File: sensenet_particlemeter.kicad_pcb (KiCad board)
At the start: 2 copper layers, 63.6 x 72.3 mm, 92 parts, among them J1 CONN_01X01, J10 CONN_01X01, J11 CONN_01X01, J12 CONN_01X01, J13 BARREL_JACK, J14 CONN_01X01, J15 CONN_01X01, J16 CONN_01X01, J17 CONN_01X01, J18 CONN_01X01, J19 CONN_01X01, J2 CONN_01X01, J20 CONN_01X01, J3 CONN_01X01, J4 CONN_01X01, J5 CONN_01X01, J6 CONN_01X01, J7 CONN_01X06, J8 CONN_01X01, J9 CONN_01X01, P1 SMA_mini, P2 SMA_mini, Q1 Q_NPN_BCV71, SW1 SW_Push, U1 wireless_patice, U10 bme280_barebone, U11 SR4G008, U2 stm32f072, U3 QUECTEL_BC95, U4 SIM, U6 M24C04, U7 M10578-A2, U8 LD39050, U9 NCP59150, Y1 8MHz

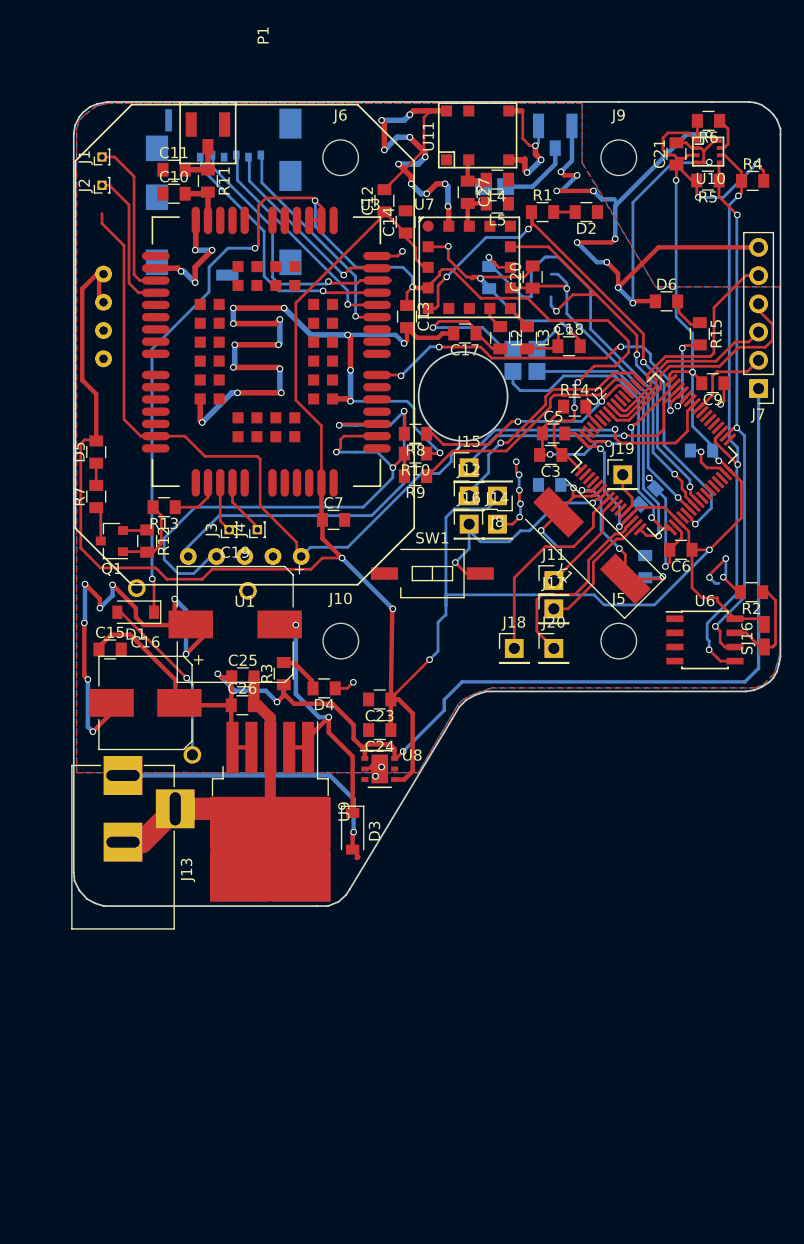
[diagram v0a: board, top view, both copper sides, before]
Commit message: added reset pin wire for quectel, fixed holes position
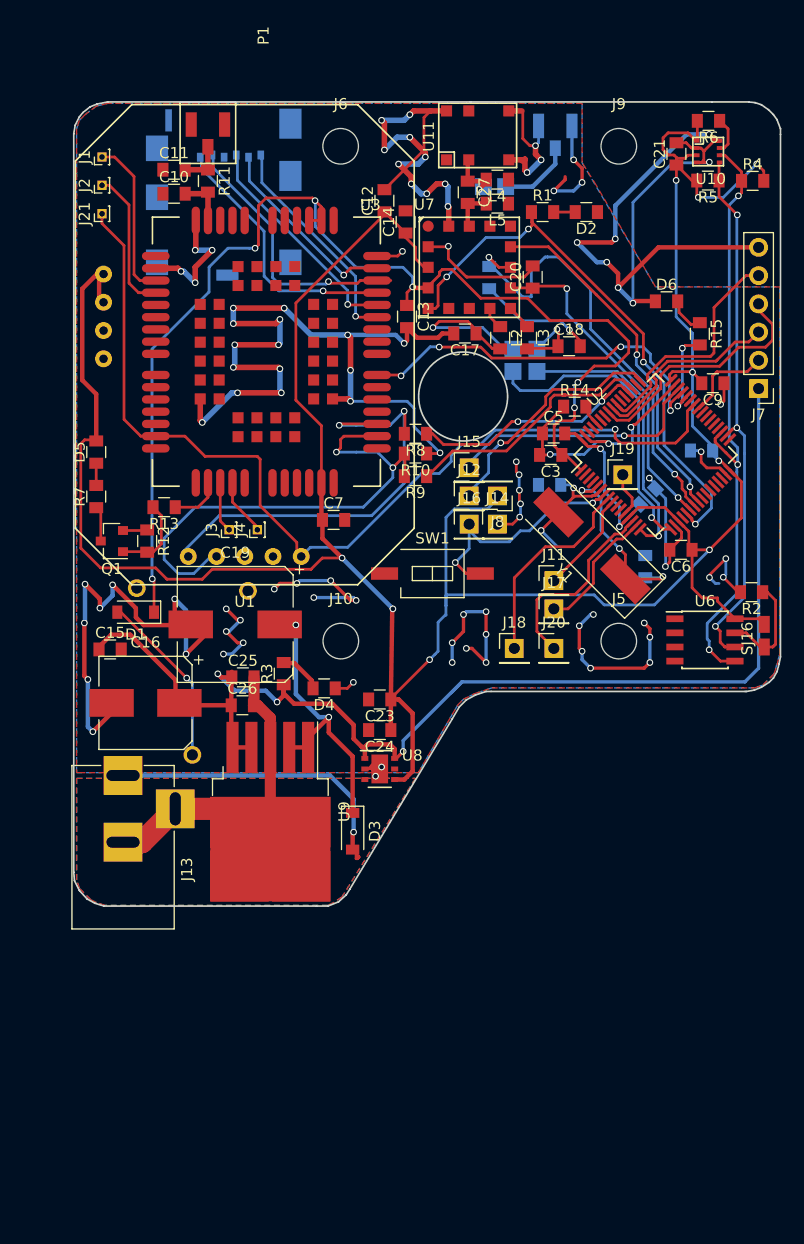
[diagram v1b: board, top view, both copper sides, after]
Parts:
- added J21: CONN_01X01, SNPM:Pin_Header_Straight_1x01_Pitch1.00mm, F.Cu at (134.6, 63.5)
- moved J6 1.03 mm to (156.1, 57.5)
- moved J9 1.03 mm to (181.1, 57.5)
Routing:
- net (no net): track 0.00 -> 48.8 mm, vias 0 -> 24
- net GND: track 408.6 -> 399.0 mm, vias 74 -> 72
- net +5V: track 112.3 -> 119.8 mm
- net gps_pulses: track 37.7 -> 32.0 mm, vias 3 -> 2
- net gps_standby: track 32.0 -> 29.8 mm
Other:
- net class Default: trace_width 0.25 -> 0.3

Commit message: lorawan module PCB added
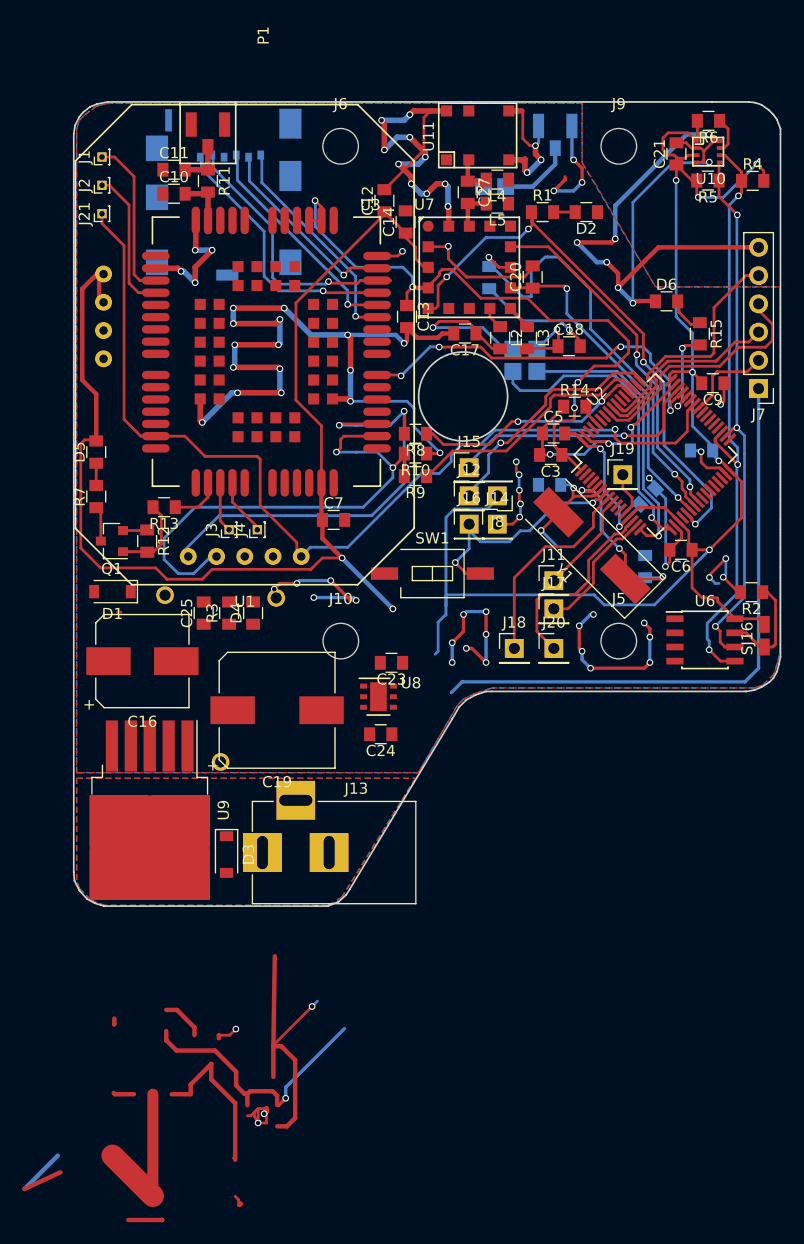
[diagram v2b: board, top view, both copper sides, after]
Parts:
- removed C15: 1u, SNPM:SMD_0805
- removed C26: 220n, SNPM:SMD_0805
- C16: value 470u -> 220n
- C19: value 220u -> 470u
- C23, C25: value 1u -> 10u
- moved J13 14.3 mm to (149.0, 121.0), turned to 180 degrees
- moved D3 11.5 mm to (145.8, 121.2)
- moved U9 10.8 mm to (138.9, 117.2)
- moved D4 9.31 mm to (148.2, 99.4), turned to 90 degrees
- moved C19 8.59 mm to (150.4, 108.2), turned to 0 degrees
- moved R3 7.34 mm to (146.1, 99.4)
- moved C25 6.77 mm to (143.8, 99.4), turned to 90 degrees
- moved U8 6.50 mm to (159.5, 107.0)
- moved C16 3.77 mm to (138.3, 103.8), turned to 0 degrees
- moved C23 3.46 mm to (160.7, 103.9)
- moved D1 2.79 mm to (135.6, 97.5)
- moved BT1 2.62 mm to (145.3, 108.1)
- moved C24 0.39 mm to (159.7, 110.3)
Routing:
- net (no net): track 48.8 -> 162.4 mm
- net GND: track 399.0 -> 299.2 mm, vias 72 -> 61
- net +5V: track 119.8 -> 53.7 mm, vias 3 -> 0
- net batt: track 107.1 -> 59.6 mm, vias 6 -> 4
- net Net-(C19-Pad1): track 29.2 -> 0.00 mm, vias 2 -> 0
- net Net-(D3-Pad2): track 27.7 -> 0.00 mm, vias 1 -> 0
- net +3V3: track 281.2 -> 255.0 mm, vias 11 -> 10
- net Net-(BT1-Pad1): track 15.8 -> 0.00 mm, vias 1 -> 0
- net Net-(D4-Pad2): track 3.88 -> 0.00 mm

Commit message: reorganized power connections
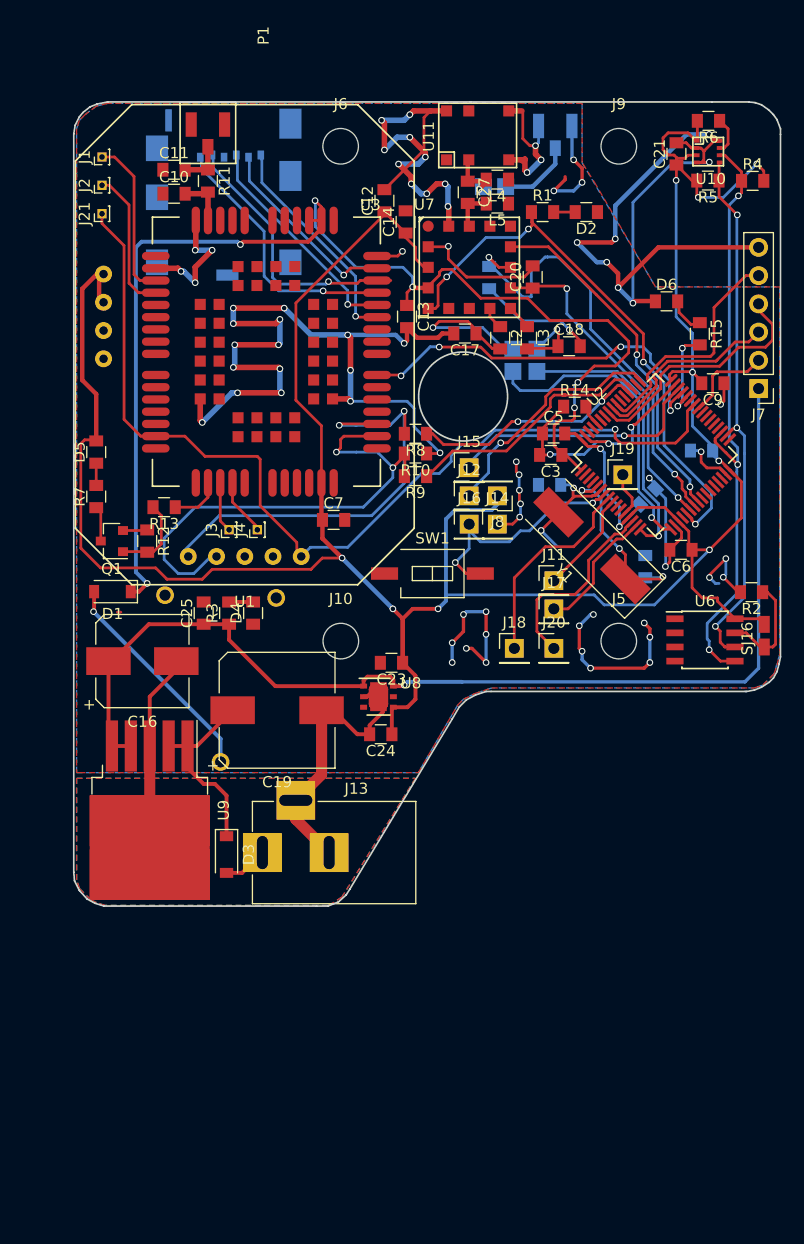
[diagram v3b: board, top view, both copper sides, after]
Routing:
- net (no net): track 162.4 -> 29.3 mm, vias 24 -> 14
- net GND: track 299.2 -> 350.0 mm
- net batt: track 59.6 -> 110.3 mm, vias 4 -> 6
- net +5V: track 53.7 -> 99.6 mm, vias 0 -> 1
- net Net-(BT1-Pad1): track 0.00 -> 20.1 mm, vias 0 -> 1
- net Net-(C19-Pad1): track 0.00 -> 17.2 mm
- net +3V3: track 255.0 -> 271.8 mm, vias 10 -> 11
- net Net-(D3-Pad2): track 0.00 -> 3.98 mm
- net Net-(D4-Pad2): track 0.00 -> 2.16 mm
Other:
- net class Default: trace_width 0.3 -> 1
